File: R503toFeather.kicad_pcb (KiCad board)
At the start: 2 copper layers, 4 parts, among them J1 MX1.0 6P

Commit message: RP2350 HSTX Production Version
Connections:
- A1 pad 16: Net-(A1-SPARE) -> (no net)
- A1 pad 17: unconnected-(A1-SDA-Pad17) -> Net-(A1-SPARE)
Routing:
- net Net-(A1-SPARE): track 11.3 -> 31.8 mm
- net VCC: track 61.0 -> 58.6 mm
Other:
- board text added: "Grow R503Pro Feather V1.0"

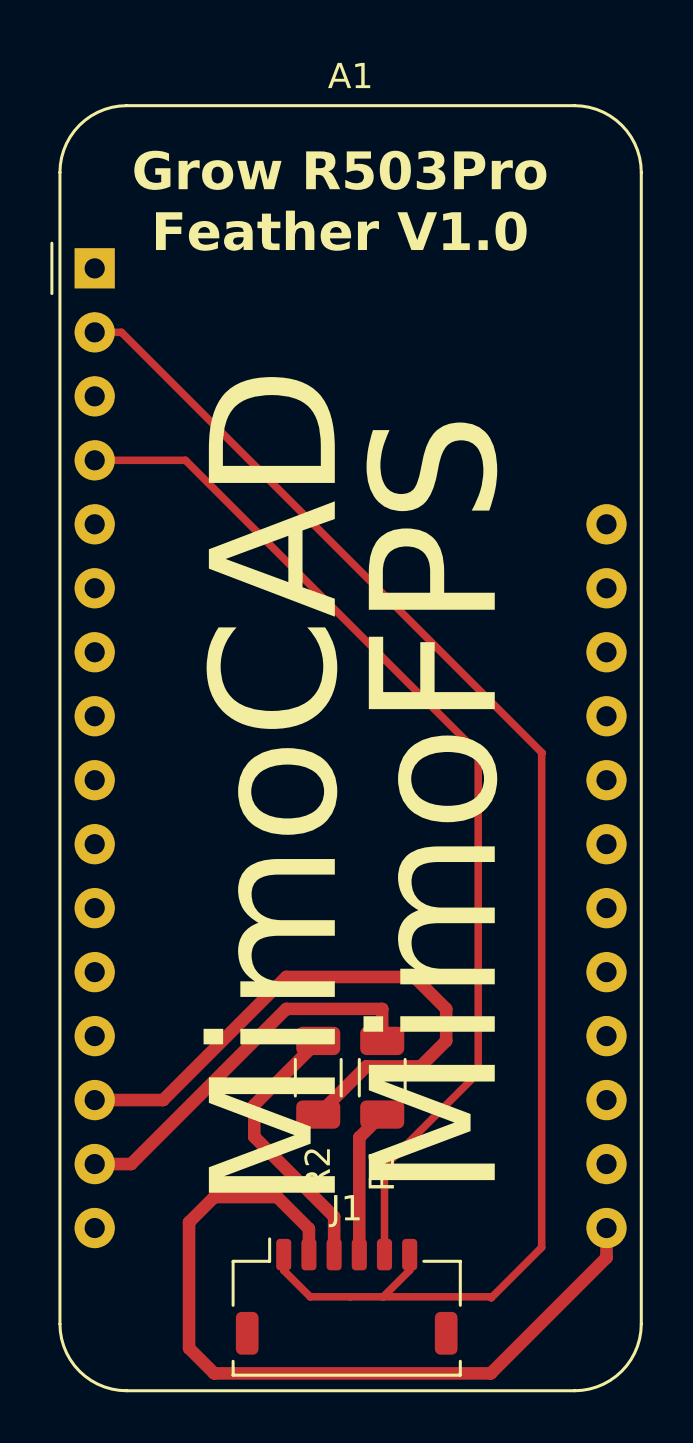
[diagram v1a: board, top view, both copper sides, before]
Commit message: Fixed J1's 2 Pin. Corrected to GND.
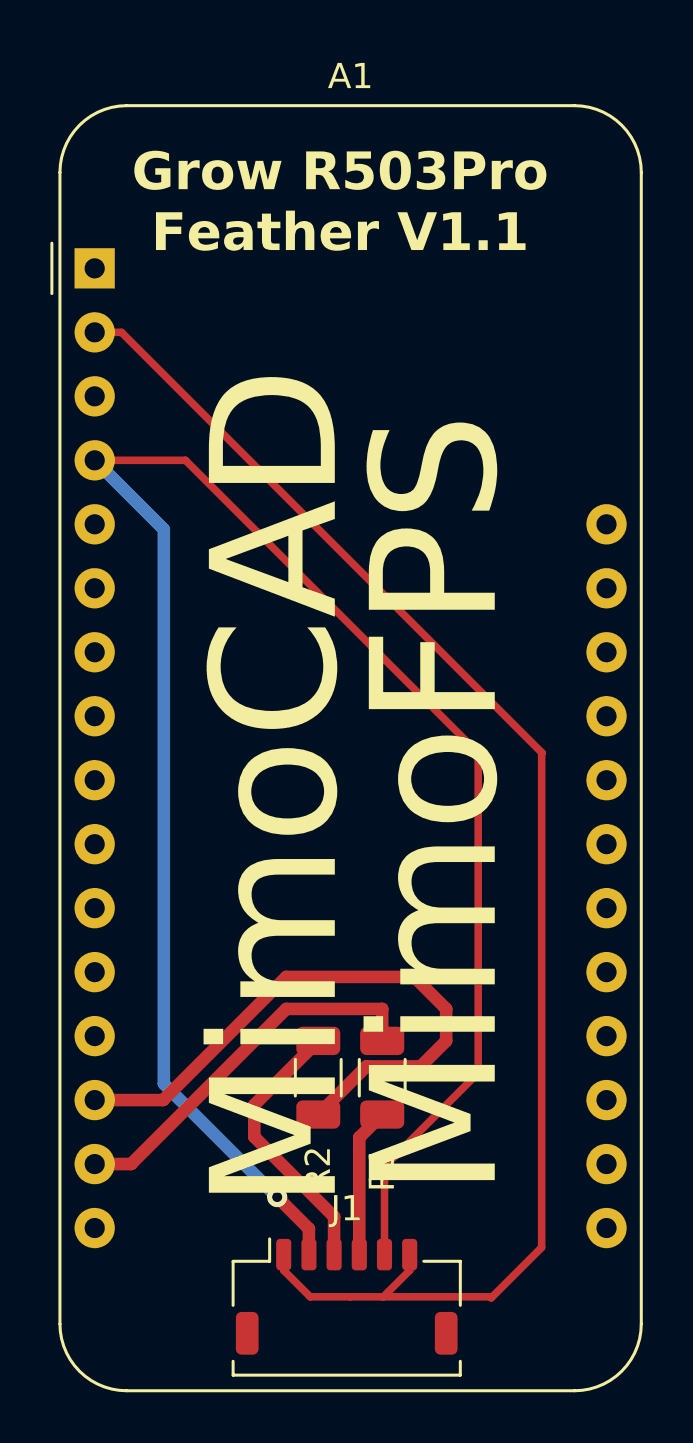
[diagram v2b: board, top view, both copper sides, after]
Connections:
- J1 pad 2: Net-(A1-SPARE) -> GND
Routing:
- net GND: track 41.5 -> 76.6 mm, vias 0 -> 1
- net Net-(A1-SPARE): track 31.8 -> 0.00 mm
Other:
- board text added: "Grow R503Pro Feather V1.1"
- board text removed: "Grow R503Pro Feather V1.0"
